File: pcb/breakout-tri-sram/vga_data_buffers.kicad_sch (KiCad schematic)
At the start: 24 parts, among them U401 74LCX541FT, U402 74LCX541FT, U403 74LCX541FT, U404 74LCX541FT, U405 74LCX541FT, U406 74LCX541FT

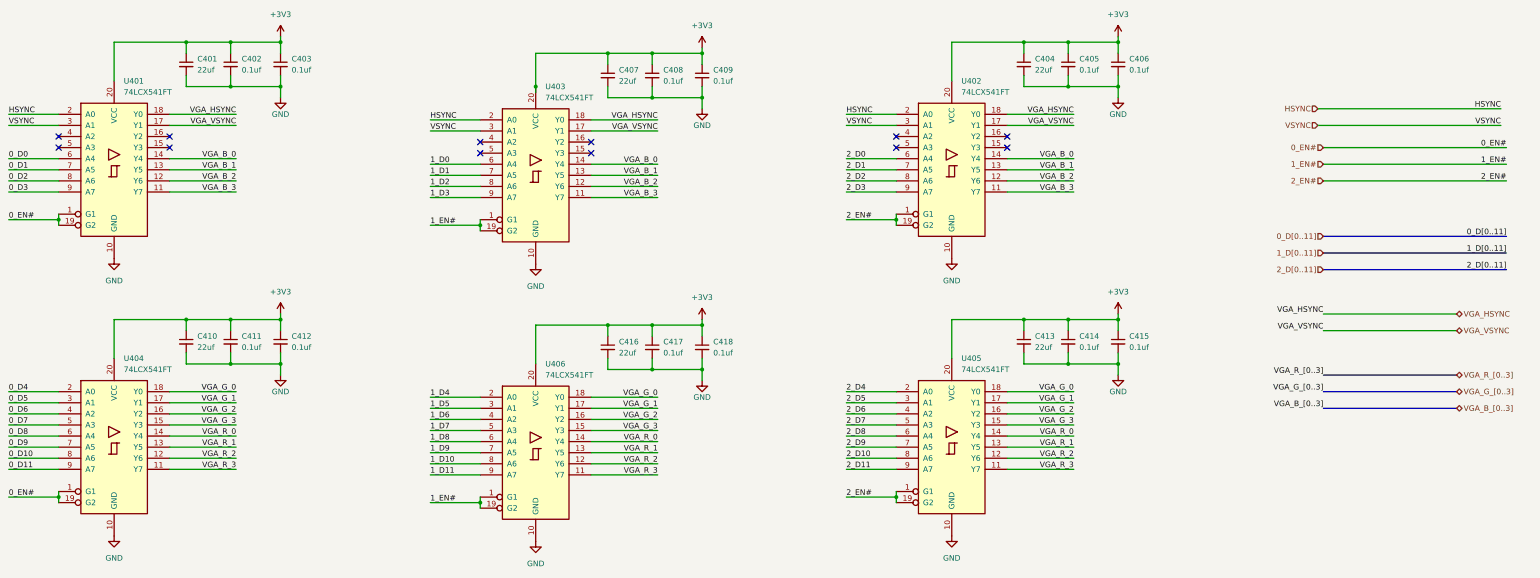
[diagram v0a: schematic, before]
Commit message: [pci][pci-sram] move to latched buffers
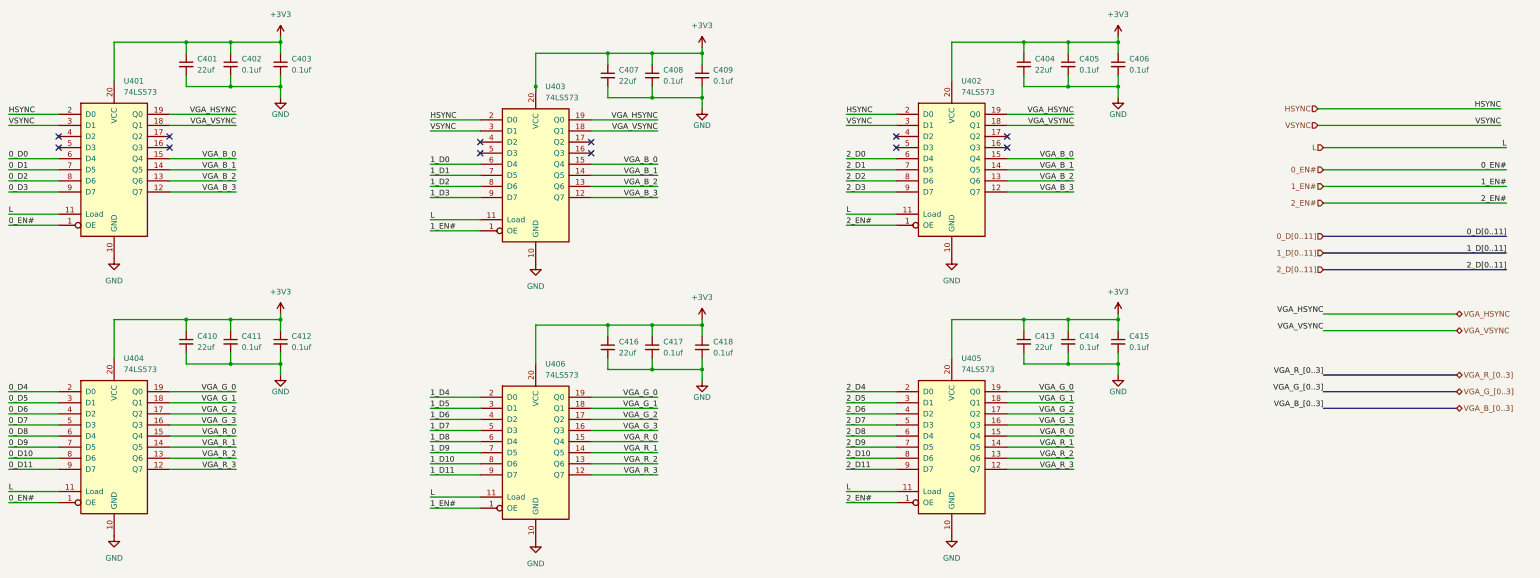
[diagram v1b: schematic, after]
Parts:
- U401, U402, U403, U404, U405, U406: value 74LCX541FT -> 74LS573; symbol 74xx:74LS541 -> 74xx:74LS573
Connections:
- net 0_EN#: no longer U401.19 (G2), U404.19 (G2)
- net 1_EN#: no longer U403.19 (G2), U406.19 (G2)
- net 2_EN#: no longer U402.19 (G2), U405.19 (G2)
- net VGA_B_0: now also U401.15 (Q4), U402.15 (Q4), U403.15 (Q4); no longer U401.14 (Y4), U402.14 (Y4), U403.14 (Y4)
- net VGA_B_1: now also U401.14 (Q5), U402.14 (Q5), U403.14 (Q5); no longer U401.13 (Y5), U402.13 (Y5), U403.13 (Y5)
- net VGA_B_2: now also U401.13 (Q6), U402.13 (Q6), U403.13 (Q6); no longer U401.12 (Y6), U402.12 (Y6), U403.12 (Y6)
- net VGA_B_3: now also U401.12 (Q7), U402.12 (Q7), U403.12 (Q7); no longer U401.11 (Y7), U402.11 (Y7), U403.11 (Y7)
- net VGA_G_0: now also U404.19 (Q0), U405.19 (Q0), U406.19 (Q0); no longer U404.18 (Y0), U405.18 (Y0), U406.18 (Y0)
- net VGA_G_1: now also U404.18 (Q1), U405.18 (Q1), U406.18 (Q1); no longer U404.17 (Y1), U405.17 (Y1), U406.17 (Y1)
- net VGA_G_2: now also U404.17 (Q2), U405.17 (Q2), U406.17 (Q2); no longer U404.16 (Y2), U405.16 (Y2), U406.16 (Y2)
- net VGA_G_3: now also U404.16 (Q3), U405.16 (Q3), U406.16 (Q3); no longer U404.15 (Y3), U405.15 (Y3), U406.15 (Y3)
- net VGA_HSYNC: now also U401.19 (Q0), U402.19 (Q0), U403.19 (Q0); no longer U401.18 (Y0), U402.18 (Y0), U403.18 (Y0)
- net VGA_R_0: now also U404.15 (Q4), U405.15 (Q4), U406.15 (Q4); no longer U404.14 (Y4), U405.14 (Y4), U406.14 (Y4)
- net VGA_R_1: now also U404.14 (Q5), U405.14 (Q5), U406.14 (Q5); no longer U404.13 (Y5), U405.13 (Y5), U406.13 (Y5)
- net VGA_R_2: now also U404.13 (Q6), U405.13 (Q6), U406.13 (Q6); no longer U404.12 (Y6), U405.12 (Y6), U406.12 (Y6)
- net VGA_R_3: now also U404.12 (Q7), U405.12 (Q7), U406.12 (Q7); no longer U404.11 (Y7), U405.11 (Y7), U406.11 (Y7)
- net VGA_VSYNC: now also U401.18 (Q1), U402.18 (Q1), U403.18 (Q1); no longer U401.17 (Y1), U402.17 (Y1), U403.17 (Y1)
- new net L: U401.11 (Load), U402.11 (Load), U403.11 (Load), U404.11 (Load), U405.11 (Load), U406.11 (Load)

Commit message: [pcb][tri-sram] 3xsram routed
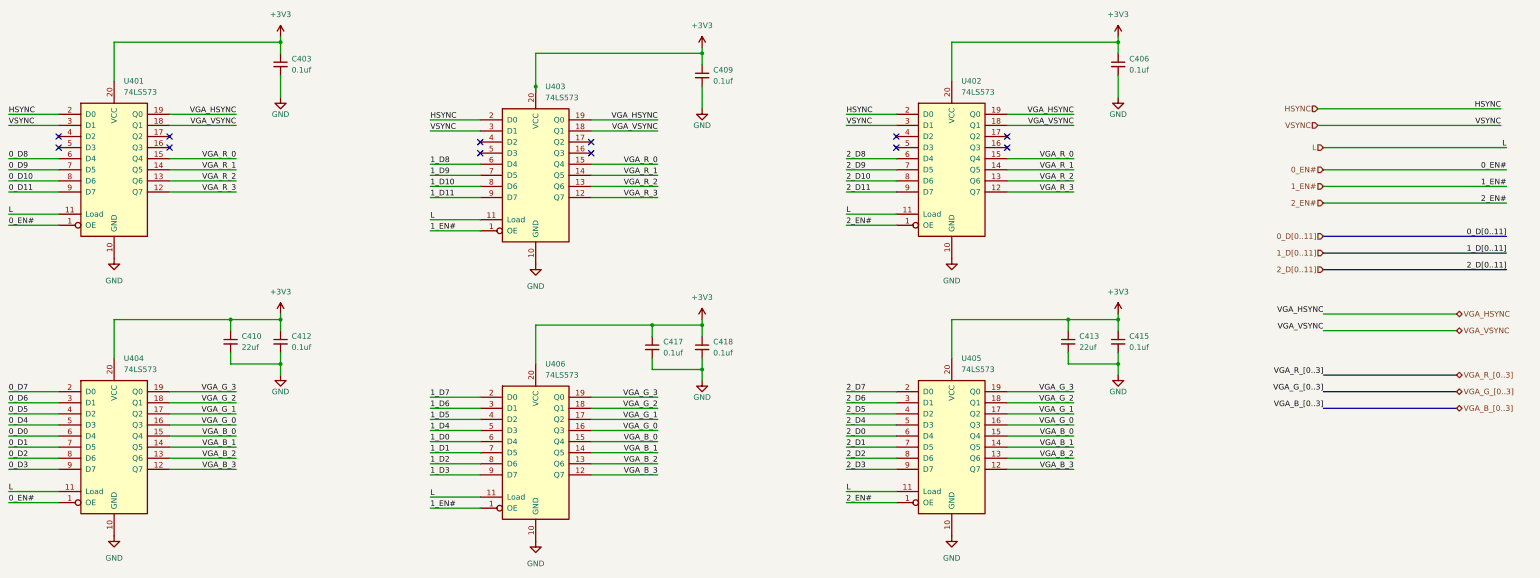
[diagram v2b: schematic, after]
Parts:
- removed C401, C404, C407, C416: 22uf, Capacitor_SMD:C_0603_1608Metric, symbol Device:C_Small
- removed C402, C405, C408, C411, C414: 0.1uf, Capacitor_SMD:C_0402_1005Metric, symbol Device:C_Small
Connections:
- net 0_D0: now also U404.6 (D4); no longer U401.6 (D4)
- net 0_D1: now also U404.7 (D5); no longer U401.7 (D5)
- net 0_D10: now also U401.8 (D6); no longer U404.8 (D6)
- net 0_D11: now also U401.9 (D7); no longer U404.9 (D7)
- net 0_D2: now also U404.8 (D6); no longer U401.8 (D6)
- net 0_D3: now also U404.9 (D7); no longer U401.9 (D7)
- net 0_D4: now also U404.5 (D3); no longer U404.2 (D0)
- net 0_D5: now also U404.4 (D2); no longer U404.3 (D1)
- net 0_D6: now also U404.3 (D1); no longer U404.4 (D2)
- net 0_D7: now also U404.2 (D0); no longer U404.5 (D3)
- net 0_D8: now also U401.6 (D4); no longer U404.6 (D4)
- net 0_D9: now also U401.7 (D5); no longer U404.7 (D5)
- net 1_D0: now also U406.6 (D4); no longer U403.6 (D4)
- net 1_D1: now also U406.7 (D5); no longer U403.7 (D5)
- net 1_D10: now also U403.8 (D6); no longer U406.8 (D6)
- net 1_D11: now also U403.9 (D7); no longer U406.9 (D7)
- net 1_D2: now also U406.8 (D6); no longer U403.8 (D6)
- net 1_D3: now also U406.9 (D7); no longer U403.9 (D7)
- net 1_D4: now also U406.5 (D3); no longer U406.2 (D0)
- net 1_D5: now also U406.4 (D2); no longer U406.3 (D1)
- net 1_D6: now also U406.3 (D1); no longer U406.4 (D2)
- net 1_D7: now also U406.2 (D0); no longer U406.5 (D3)
- net 1_D8: now also U403.6 (D4); no longer U406.6 (D4)
- net 1_D9: now also U403.7 (D5); no longer U406.7 (D5)
- net 2_D0: now also U405.6 (D4); no longer U402.6 (D4)
- net 2_D1: now also U405.7 (D5); no longer U402.7 (D5)
- net 2_D10: now also U402.8 (D6); no longer U405.8 (D6)
- net 2_D11: now also U402.9 (D7); no longer U405.9 (D7)
- net 2_D2: now also U405.8 (D6); no longer U402.8 (D6)
- net 2_D3: now also U405.9 (D7); no longer U402.9 (D7)
- net 2_D4: now also U405.5 (D3); no longer U405.2 (D0)
- net 2_D5: now also U405.4 (D2); no longer U405.3 (D1)
- net 2_D6: now also U405.3 (D1); no longer U405.4 (D2)
- net 2_D7: now also U405.2 (D0); no longer U405.5 (D3)
- net 2_D8: now also U402.6 (D4); no longer U405.6 (D4)
- net 2_D9: now also U402.7 (D5); no longer U405.7 (D5)
- net VGA_B_0: now also U404.15 (Q4), U405.15 (Q4), U406.15 (Q4); no longer U401.15 (Q4), U402.15 (Q4), U403.15 (Q4)
- net VGA_B_1: now also U404.14 (Q5), U405.14 (Q5), U406.14 (Q5); no longer U401.14 (Q5), U402.14 (Q5), U403.14 (Q5)
- net VGA_B_2: now also U404.13 (Q6), U405.13 (Q6), U406.13 (Q6); no longer U401.13 (Q6), U402.13 (Q6), U403.13 (Q6)
- net VGA_B_3: now also U404.12 (Q7), U405.12 (Q7), U406.12 (Q7); no longer U401.12 (Q7), U402.12 (Q7), U403.12 (Q7)
- net VGA_G_0: now also U404.16 (Q3), U405.16 (Q3), U406.16 (Q3); no longer U404.19 (Q0), U405.19 (Q0), U406.19 (Q0)
- net VGA_G_1: now also U404.17 (Q2), U405.17 (Q2), U406.17 (Q2); no longer U404.18 (Q1), U405.18 (Q1), U406.18 (Q1)
- net VGA_G_2: now also U404.18 (Q1), U405.18 (Q1), U406.18 (Q1); no longer U404.17 (Q2), U405.17 (Q2), U406.17 (Q2)
- net VGA_G_3: now also U404.19 (Q0), U405.19 (Q0), U406.19 (Q0); no longer U404.16 (Q3), U405.16 (Q3), U406.16 (Q3)
- net VGA_R_0: now also U401.15 (Q4), U402.15 (Q4), U403.15 (Q4); no longer U404.15 (Q4), U405.15 (Q4), U406.15 (Q4)
- net VGA_R_1: now also U401.14 (Q5), U402.14 (Q5), U403.14 (Q5); no longer U404.14 (Q5), U405.14 (Q5), U406.14 (Q5)
- net VGA_R_2: now also U401.13 (Q6), U402.13 (Q6), U403.13 (Q6); no longer U404.13 (Q6), U405.13 (Q6), U406.13 (Q6)
- net VGA_R_3: now also U401.12 (Q7), U402.12 (Q7), U403.12 (Q7); no longer U404.12 (Q7), U405.12 (Q7), U406.12 (Q7)
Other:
- moved on the sheet: C410, C413

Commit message: [pcb][tri-sram] tri-sram complete
squashed big-bus branch
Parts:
- C404: renamed from C417; value 0.1uf -> 22uf; footprint Capacitor_SMD:C_0402_1005Metric -> Capacitor_SMD:C_0603_1608Metric
- renumbered C410 to C401, C403 to C402, C412 to C403, C409 to C405, C418 to C406, C413 to C407, C406 to C408, C415 to C409, U404 to U402, U406 to U404, U402 to U405, U405 to U406
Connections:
- net 0_D0: now also U401.6 (D4); no longer U402.6 (D4)
- net 0_D1: now also U401.7 (D5); no longer U402.7 (D5)
- net 0_D10: now also U402.4 (D2); no longer U401.8 (D6)
- net 0_D11: now also U402.5 (D3); no longer U401.9 (D7)
- net 0_D2: now also U401.8 (D6); no longer U402.8 (D6)
- net 0_D3: now also U401.9 (D7); no longer U402.9 (D7)
- net 0_D4: now also U402.9 (D7); no longer U402.5 (D3)
- net 0_D5: now also U402.8 (D6); no longer U402.4 (D2)
- net 0_D6: now also U402.7 (D5); no longer U402.3 (D1)
- net 0_D7: now also U402.6 (D4); no longer U402.2 (D0)
- net 0_D8: now also U402.2 (D0); no longer U401.6 (D4)
- net 0_D9: now also U402.3 (D1); no longer U401.7 (D5)
- net 1_D0: now also U403.6 (D4); no longer U404.6 (D4)
- net 1_D1: now also U403.7 (D5); no longer U404.7 (D5)
- net 1_D10: now also U404.4 (D2); no longer U403.8 (D6)
- net 1_D11: now also U404.5 (D3); no longer U403.9 (D7)
- net 1_D2: now also U403.8 (D6); no longer U404.8 (D6)
- net 1_D3: now also U403.9 (D7); no longer U404.9 (D7)
- net 1_D4: now also U404.9 (D7); no longer U404.5 (D3)
- net 1_D5: now also U404.8 (D6); no longer U404.4 (D2)
- net 1_D6: now also U404.7 (D5); no longer U404.3 (D1)
- net 1_D7: now also U404.6 (D4); no longer U404.2 (D0)
- net 1_D8: now also U404.2 (D0); no longer U403.6 (D4)
- net 1_D9: now also U404.3 (D1); no longer U403.7 (D5)
- net 2_D0: now also U405.6 (D4); no longer U406.6 (D4)
- net 2_D1: now also U405.7 (D5); no longer U406.7 (D5)
- net 2_D10: now also U406.4 (D2); no longer U405.8 (D6)
- net 2_D11: now also U406.5 (D3); no longer U405.9 (D7)
- net 2_D2: now also U405.8 (D6); no longer U406.8 (D6)
- net 2_D3: now also U405.9 (D7); no longer U406.9 (D7)
- net 2_D4: now also U406.9 (D7); no longer U406.5 (D3)
- net 2_D5: now also U406.8 (D6); no longer U406.4 (D2)
- net 2_D6: now also U406.7 (D5); no longer U406.3 (D1)
- net 2_D7: now also U406.6 (D4); no longer U406.2 (D0)
- net 2_D8: now also U406.2 (D0); no longer U405.6 (D4)
- net 2_D9: now also U406.3 (D1); no longer U405.7 (D5)
- removed net HSYNC: U401.2 (D0), U403.2 (D0), U405.2 (D0)
- net VGA_B_0 renamed VGA_G3
- net VGA_B_1 renamed VGA_G2
- net VGA_B_2 renamed VGA_G1
- net VGA_B_3 renamed VGA_G0
- net VGA_G_0 renamed VGA_R3
- net VGA_G_1 renamed VGA_R2
- net VGA_G_2 renamed VGA_R1
- net VGA_G_3 renamed VGA_R0
- removed net VGA_HSYNC: U401.19 (Q0), U403.19 (Q0), U405.19 (Q0)
- net VGA_R_0 renamed VGA_B0
- net VGA_R_1 renamed VGA_B1
- net VGA_R_2 renamed VGA_B2
- net VGA_R_3 renamed VGA_B3
- removed net VGA_VSYNC: U401.18 (Q1), U403.18 (Q1), U405.18 (Q1)
- removed net VSYNC: U401.3 (D1), U403.3 (D1), U405.3 (D1)
- no-connect marks 12 -> 24
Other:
- moved on the sheet: C404, C405, C406, U403, U404

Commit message: [pcb][tri-sram] add part numbers
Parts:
- C404: Digi-Key Part Number 490-6328-1-ND -> 490-7611-1-ND; LCSC Part # C1525 -> C59461
- U401, U402, U403, U404, U405, U406: Digi-Key Part Number (none) -> 264-74LCX541FT(AE)CT-ND
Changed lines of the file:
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@@
+			)
+		)
+		(property "Digi-Key Part Number" "264-74LCX541FT(AE)CT-ND"
+			(at 175.26 160.02 0)
+			(effects
+				(font
+					(size 1.27 1.27)
+				)
+				(hide yes)
 			)
 		)
@@
 			)
 		)
+		(property "Digi-Key Part Number" "264-74LCX541FT(AE)CT-ND"
+			(at 78.74 96.52 0)
+			(effects
+				(font
+					(size 1.27 1.27)
+				)
+				(hide yes)
+			)
+		)
 		(pin "5"
 		)
@@
 			)
 		)
+		(property "Digi-Key Part Number" "264-74LCX541FT(AE)CT-ND"
+			(at 270.51 160.02 0)
+			(effects
+				(font
+					(size 1.27 1.27)
+				)
+				(hide yes)
+			)
+		)
 		(pin "5"
 		)
@@
 			)
 		)
+		(property "Digi-Key Part Number" "264-74LCX541FT(AE)CT-ND"
+			(at 175.26 96.52 0)
+			(effects
+				(font
+					(size 1.27 1.27)
+				)
+				(hide yes)
+			)
+		)
 		(pin "5"
 		)
@@
 			)
 		)
+		(property "Digi-Key Part Number" "264-74LCX541FT(AE)CT-ND"
+			(at 270.51 96.52 0)
+			(effects
+				(font
+					(size 1.27 1.27)
+				)
+				(hide yes)
+			)
+		)
 		(pin "5"
 		)
@@
 			)
 		)
+		(property "Digi-Key Part Number" "264-74LCX541FT(AE)CT-ND"
+			(at 78.74 160.02 0)
+			(effects
+				(font
+					(size 1.27 1.27)
+				)
+				(hide yes)
+			)
+		)
 		(pin "5"
 		)
@@
 			)
 		)
-		(property "LCSC Part #" "C1525"
+		(property "LCSC Part #" "C59461"
 			(at 201.93 135.89 0)
 			(effects
@@
 			)
 		)
-		(property "Digi-Key Part Number" "490-6328-1-ND"
+		(property "Digi-Key Part Number" "490-7611-1-ND"
 			(at 201.93 135.89 0)
 			(effects
